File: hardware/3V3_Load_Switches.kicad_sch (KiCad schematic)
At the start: 28 parts, among them Q18 SI2302DDS-T1-GE3, Q19 SI2302DDS-T1-GE3, Q20 SI2302DDS-T1-GE3, U1 LMV321RIYLT, U2 INA199C3DCKR, U3 INA199C3DCKR, U4 INA199C1DCKR, U5 NVTFS5116PLTAG, U6 NVTFS5116PLTAG, U7 NVTFS5116PLTAG

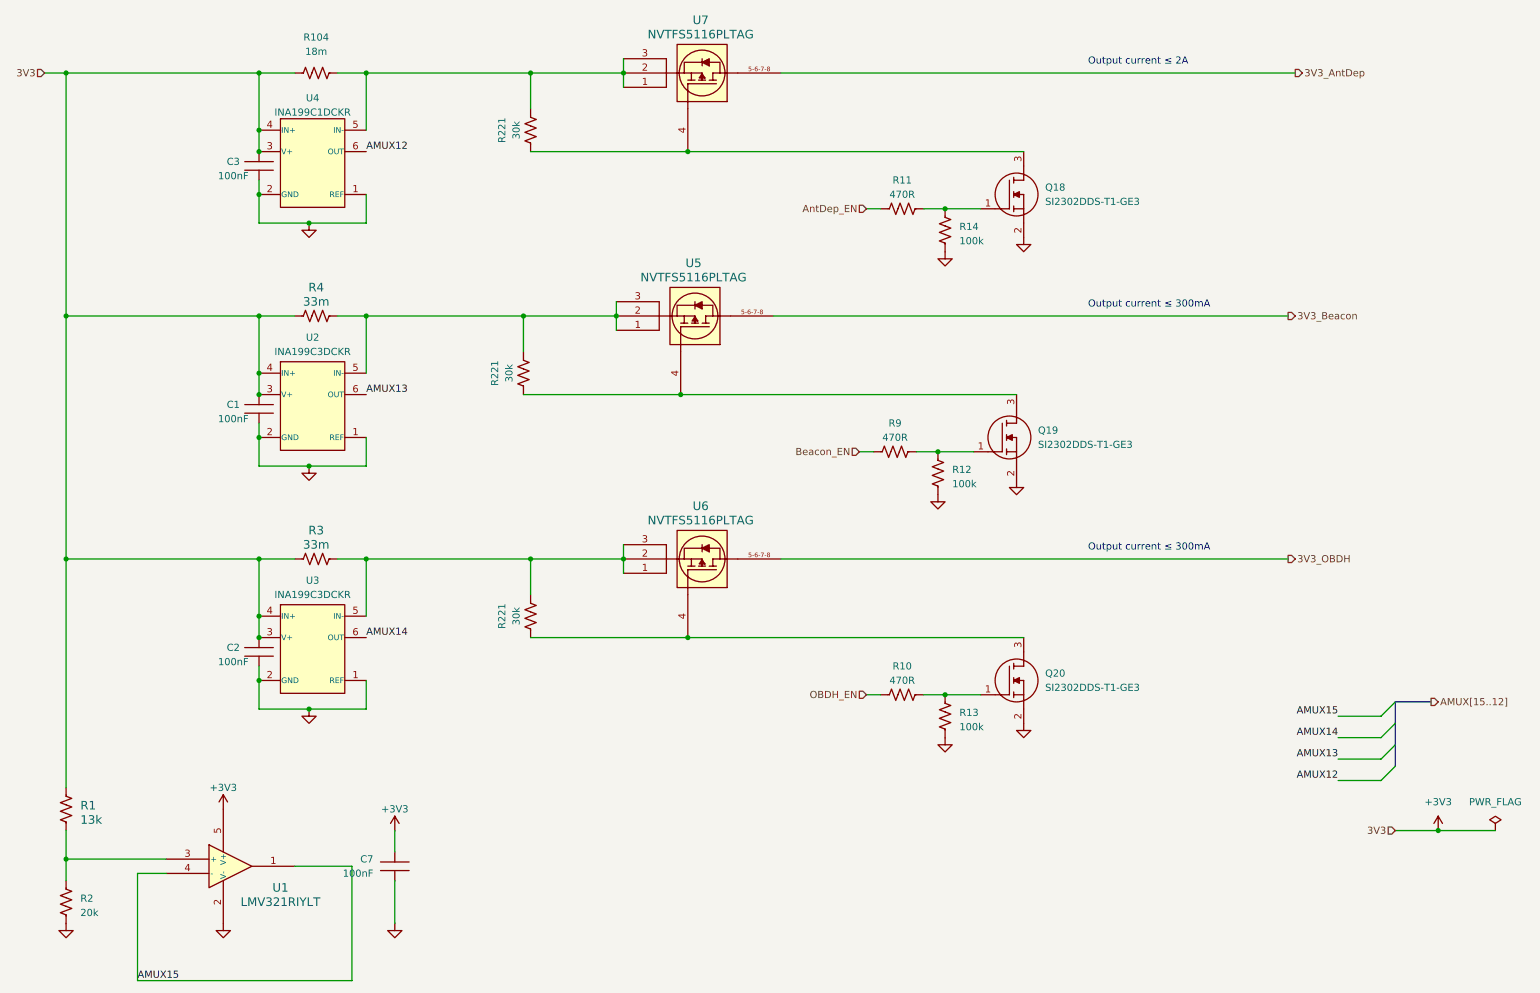
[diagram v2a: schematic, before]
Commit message: hardware: Updating the schematic and layout to solve #8, #9 and #10.
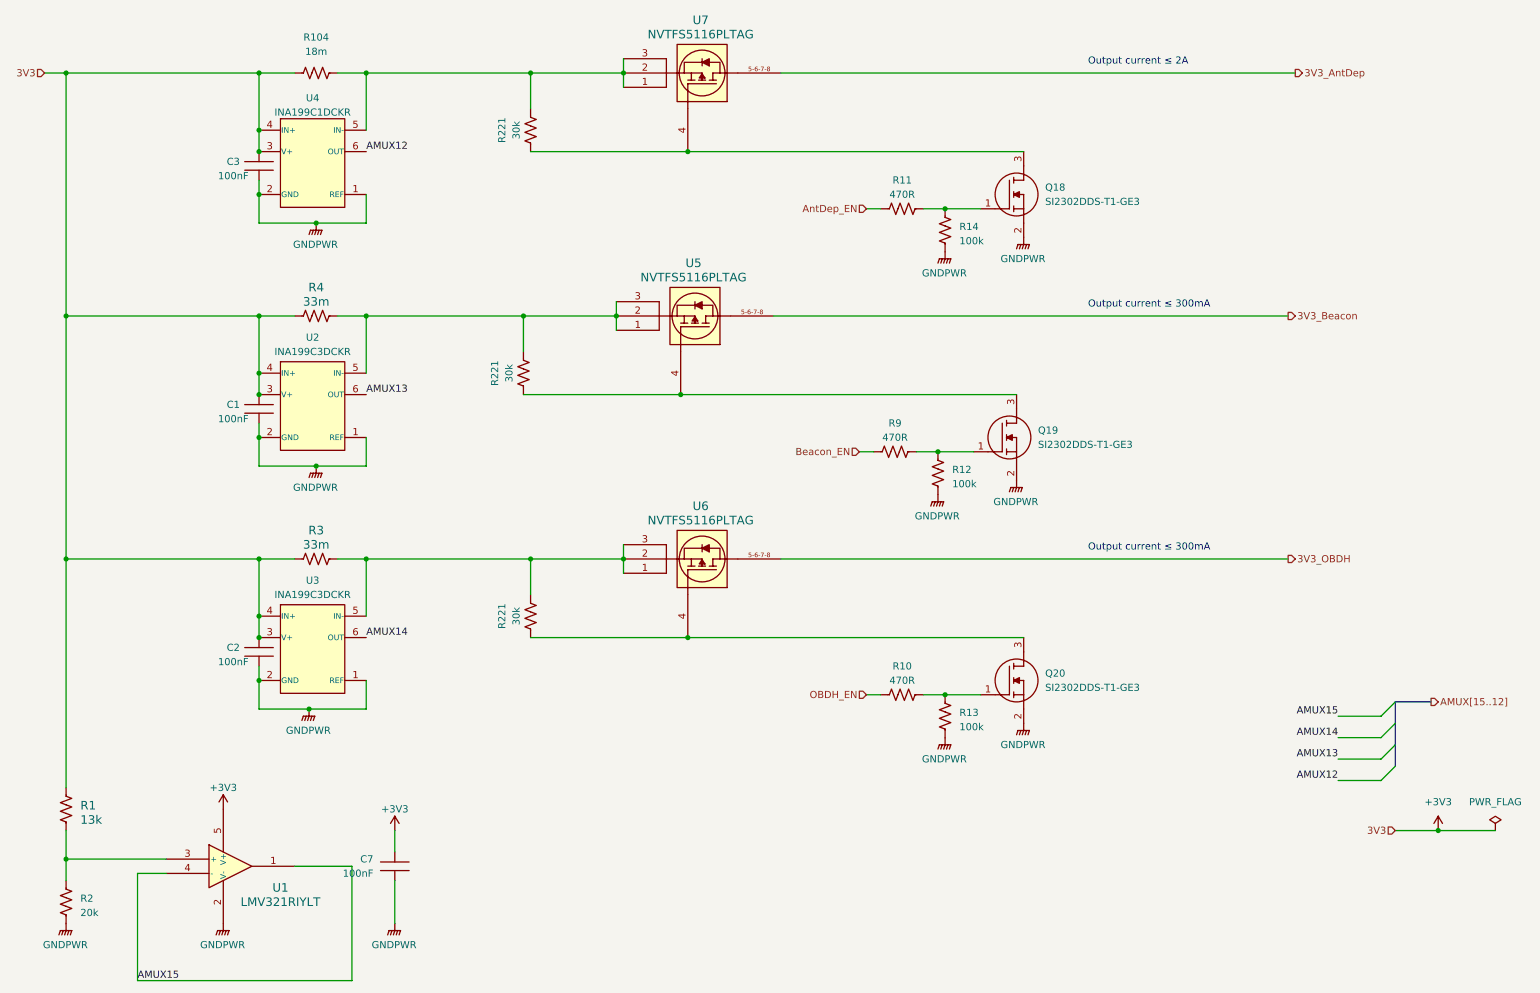
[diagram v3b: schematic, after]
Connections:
- net GND renamed GNDPWR

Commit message: hardware: Updating the MPPT circuit.
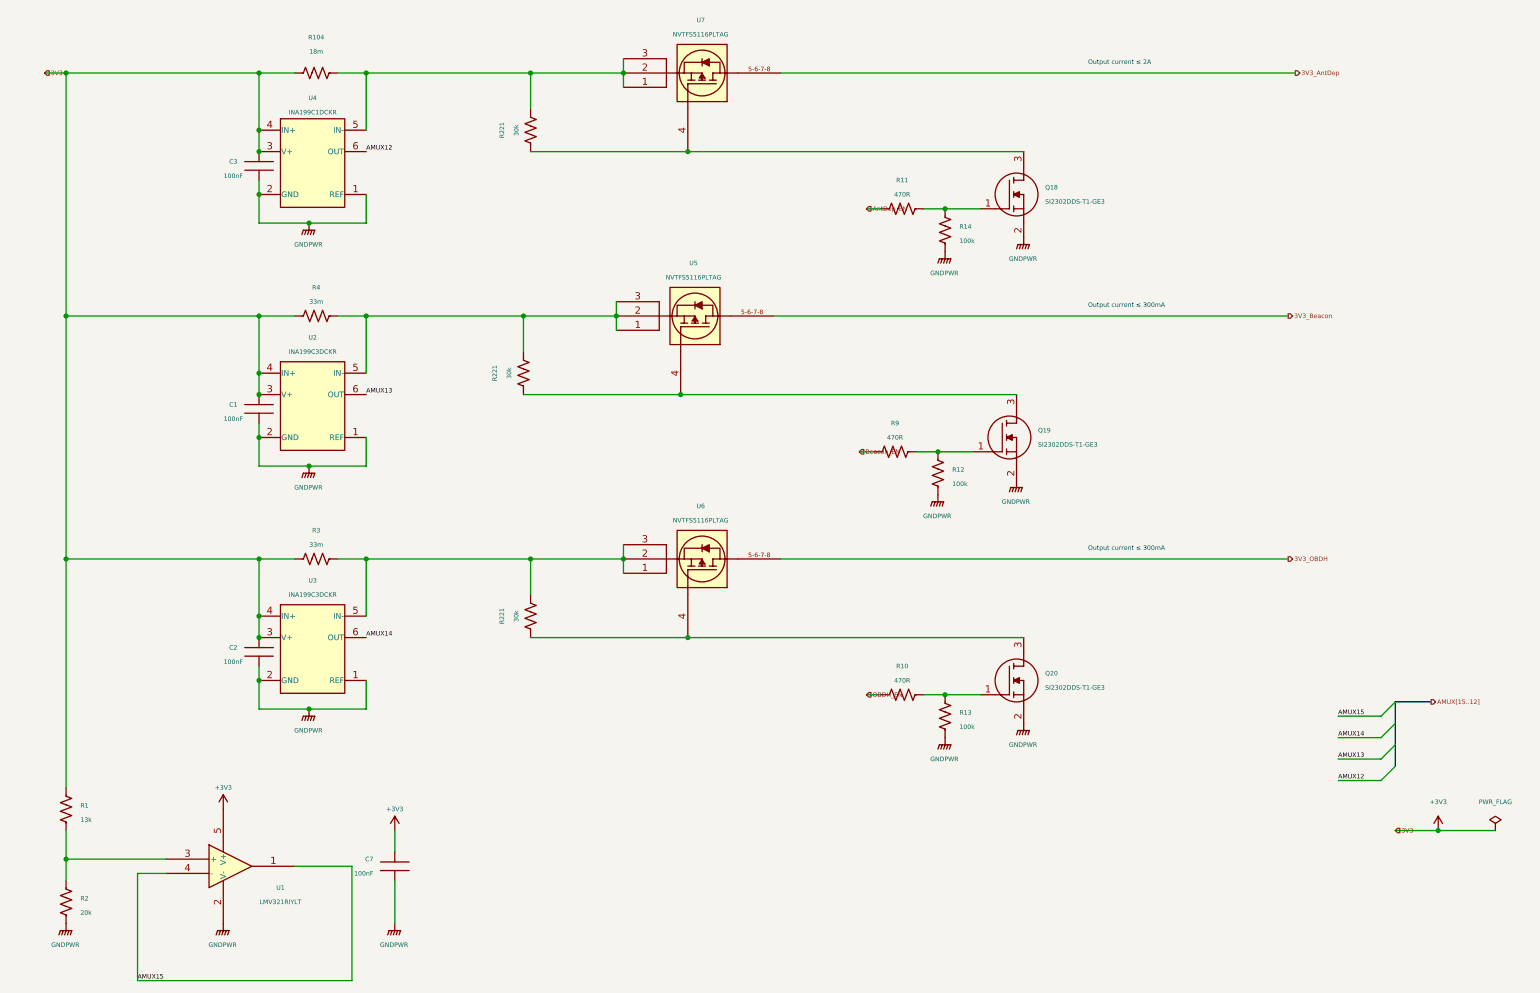
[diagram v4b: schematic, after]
